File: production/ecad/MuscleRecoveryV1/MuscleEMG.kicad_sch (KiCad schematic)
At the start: 0 parts

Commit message: changes to fuel guage schematic and quick draft of ecg schematic - not finished
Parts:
- added C1, C2: 470n, symbol Device:C
- added C10, C4: 1n, symbol Device:C
- added C11: 100n, symbol Device:C
- added C3: 270p, symbol Device:C
- added D5, D6: LED, symbol Device:LED
- added J1: electrode 1, symbol Connector:Screw_Terminal_01x01
- added J2: electrode 2, symbol Connector:Screw_Terminal_01x01
- added J3: electrode 3, symbol Connector:Screw_Terminal_01x01
- added R1, R2: 200k, symbol Device:R
- added R19, R22: 180K, symbol Device:R
- added R20, R21: 2.2M, symbol Device:R
- added R23: 390K, symbol Device:R
- added R24, R28: 180, symbol Device:R
- added R25, R26, R5, R6: 1M, symbol Device:R
- added R27: 10k, symbol Device:R
- added R3: 27k, symbol Device:R
- added R4: 330k, symbol Device:R
- added R7: 100k, symbol Device:R
- added U5: AD8232ACPZ-R7, CP_20_10_ADI, symbol AD8232ACPZ-R7:AD8232ACPZ-R7
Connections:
- new net: C3.2, R4.2, R5.1
- new net: C1.1, U5.1 (HPDRIVE)
- new net: R27.1, U5.13 (*SDN)
- new net: R25.2, R26.1, U5.18 (REFIN)
- new net: R19.2, U5.2 (IN+)
- new net: C1.2, R1.1, U5.20 (HPSENSE)
- new net: R22.2, U5.3 (IN-)
- new net: C10.1, U5.4 (RLDFB)
- new net: C10.2, R23.2, U5.5 (RLD)
- new net: C4.2, R5.2, U5.7 (OPAMP+)
- new net: R6.2, R7.2, U5.9 (OPAMP-)
- new net: D6.1 (K), R28.1
- new net: J2.1 (Pin_1), R21.1, R22.1
- new net: D5.1 (K), R24.1
- new net: R1.2, R2.2, R3.1
- new net: J3.1 (Pin_1), R23.1
- new net: J1.1 (Pin_1), R19.1, R20.1
- new net GND: C11.2, R24.2, R26.2, R28.2, U5.14 (AC/*DC), U5.16 (GND)
- new net HP: R2.1, R4.1, U5.19 (IAOUT)
- new net REF: C2.2, C4.1, R7.1, U5.8 (REFOUT)
- new net SW: C2.1, R3.2, U5.6 (SW)
- new net VCC: C11.1, D6.2 (A), R20.2, R21.2, R25.1, R27.2, U5.15 (FR), U5.17 (VS+)
- new net Vout: C3.1, D5.2 (A), R6.1, U5.10 (OUT)
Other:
- note added: "High Pass: Fc = 10/(2piSQRT(R1R2C1C2)) R3 = 0.14R1"
- note added: "Low Pass: Fc = 10/(2piSQRT(R4R5C3C4)) Gain = 1 + R6 / R7"

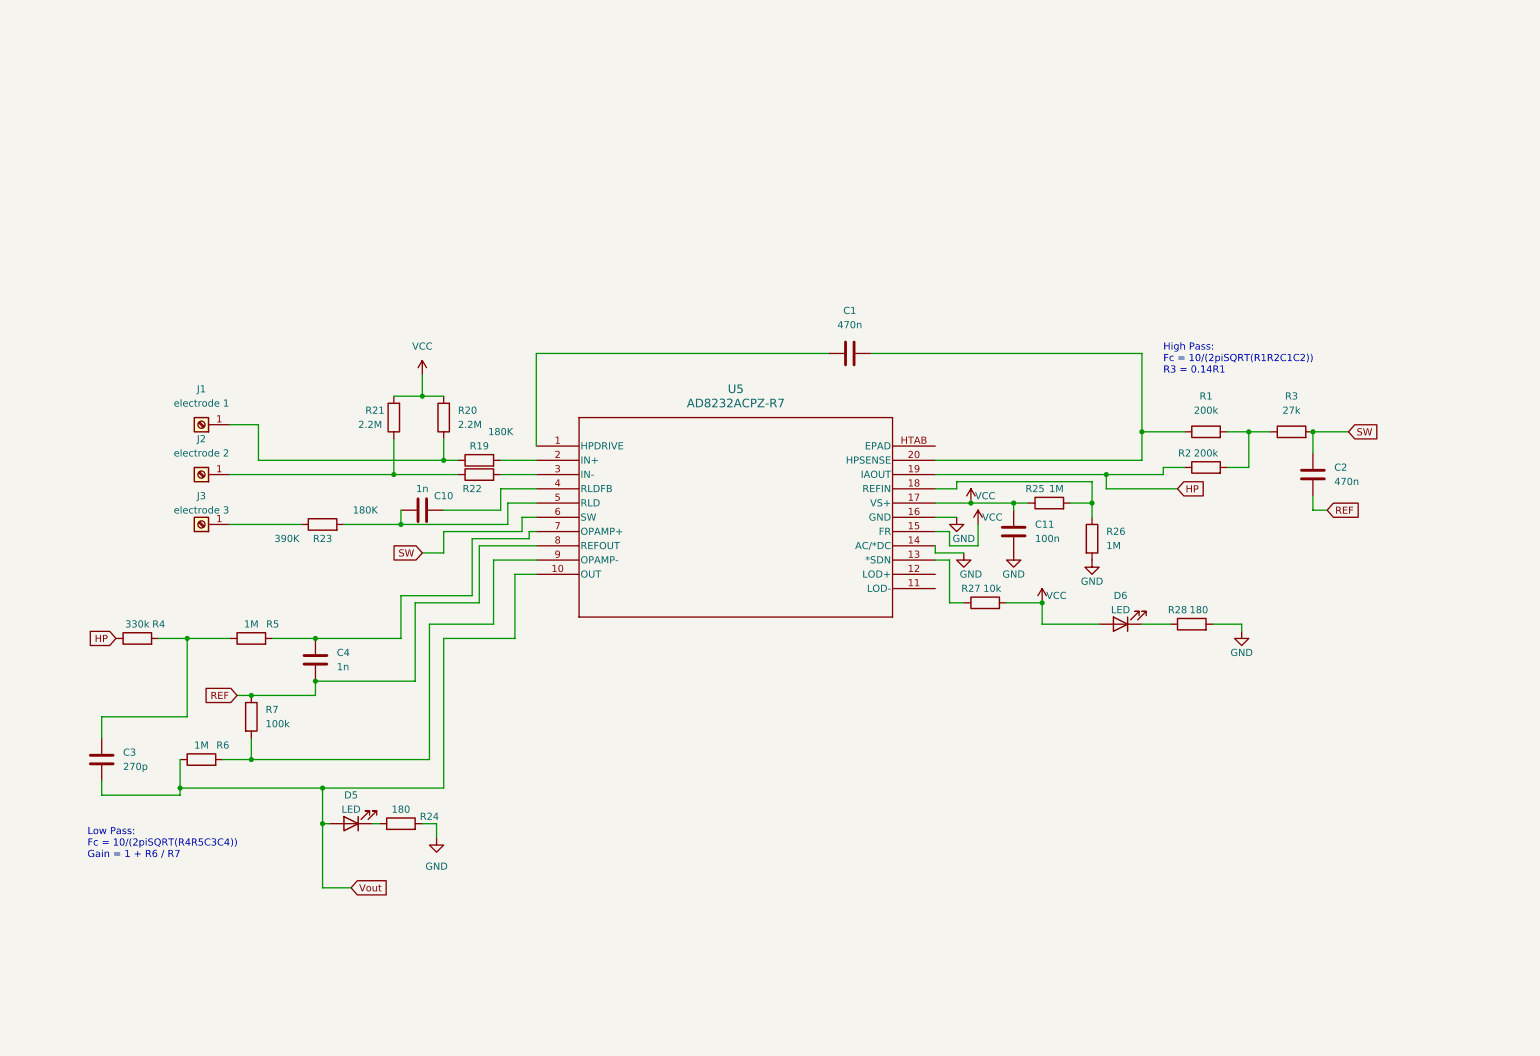
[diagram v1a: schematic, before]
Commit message: added ADS1115 schematic
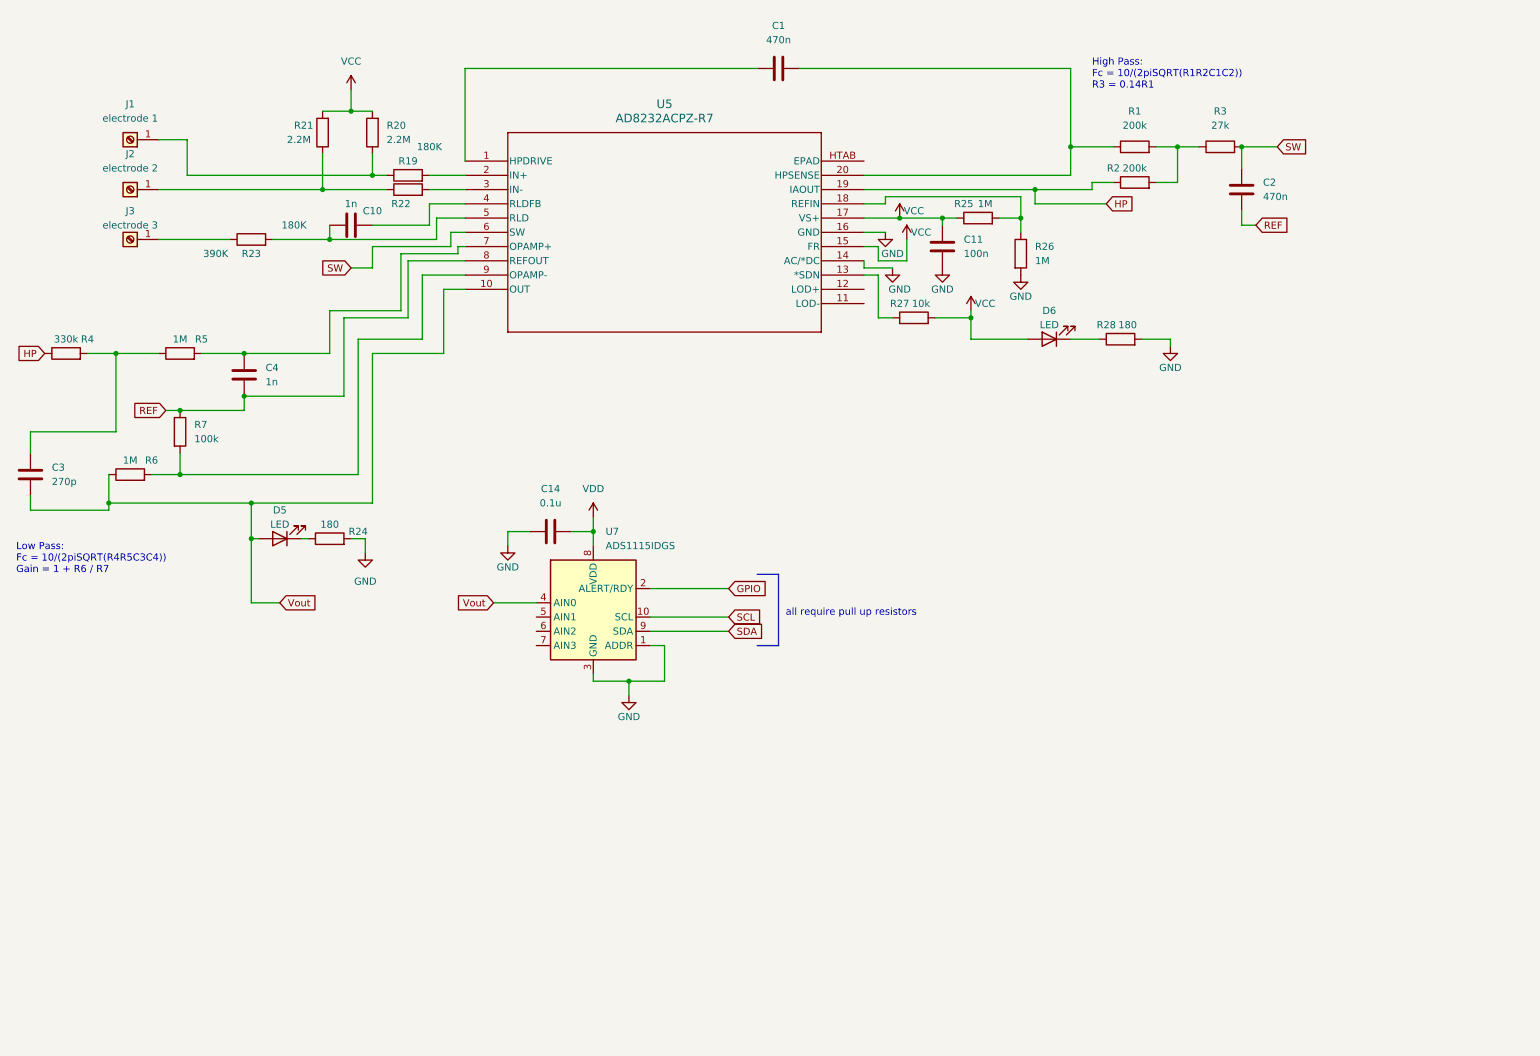
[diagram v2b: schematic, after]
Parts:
- added C14: 0.1u, symbol Device:C
- added U7: ADS1115IDGS, Package_SO:TSSOP-10_3x3mm_P0.5mm, symbol Analog_ADC:ADS1115IDGS
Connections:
- net GND: now also C14.1, U7.1 (ADDR), U7.3 (GND)
- net Vout: now also U7.4 (AIN0)
- new net GPIO: U7.2 (ALERT/RDY)
- new net SCL: U7.10 (SCL)
- new net SDA: U7.9 (SDA)
- new net VDD: C14.2, U7.8 (VDD)
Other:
- note added: "all require pull up resistors"
- moved on the sheet: C1, C10, C11, C2, C3, C4, D5, D6, J1, J2, J3, R1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

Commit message: cleaned up EMG
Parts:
- removed J1: electrode 1, symbol Connector:Screw_Terminal_01x01
- removed J2: electrode 2, symbol Connector:Screw_Terminal_01x01
- removed J3: electrode 3, symbol Connector:Screw_Terminal_01x01
- added J1: AudioJack3, symbol Connector_Audio:AudioJack3
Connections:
- net GND: now also U5.HTAB (EPAD)
- net RA: now reaches R21.1, R22.1
- net RA: now also J1.R
- net RL: now reaches R23.1
- net RL: now also J1.T
- net LA: now reaches R19.1, R20.1
- net LA: now also J1.S
- net VCC renamed +3V3
- no-connect marks 0 -> 2
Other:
- note added: "Audiojack. Connections must be configured."
- note added: "currently at 16.93Hz"
- note added: "currently at 533.189Hz"
- moved on the sheet: C1, C10, C11, C14, C2, C3, C4, D5, D6, R1, R19, R2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

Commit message: Labels and other stuff
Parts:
- added J2: Screw_Terminal_01x03, symbol Connector:Screw_Terminal_01x03
- added R29: 4.7k, symbol Device:R
- added Vout1: TestPoint, symbol Connector:TestPoint
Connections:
- net VDD is gone; now on net +3V3: C14.2, U7.8 (VDD)
- net +3V3: now also R29.1
- net LA: now also J2.3 (Pin_3)
- net RA: now also J2.2 (Pin_2)
- net RL: now also J2.1 (Pin_1)
- net Vout: now also Vout1.1
- net GPIO renamed ALERT/READY
- net ALERT/READY: now also R29.2
- no-connect marks 2 -> 5
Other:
- note added: "AD8232 Circuit"
- note added: "ADC"
- moved on the sheet: C1, C10, C11, C14, C2, C3, C4, D5, D6, J1, R1, R19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

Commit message: Display commit 1
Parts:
- removed J1: AudioJack3, symbol Connector_Audio:AudioJack3
- removed J2: Screw_Terminal_01x03, symbol Connector:Screw_Terminal_01x03
- removed R29: 4.7k, symbol Device:R
- removed Vout1: TestPoint, symbol Connector:TestPoint
- added J1: electrode 1, symbol Connector:Screw_Terminal_01x01
- added J2: electrode 2, symbol Connector:Screw_Terminal_01x01
- added J3: electrode 3, symbol Connector:Screw_Terminal_01x01
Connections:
- net GND: no longer U5.HTAB (EPAD)
- net +3V3 renamed VCC
- net VCC: no longer C14.2, U7.8 (VDD)
- net ALERT/READY renamed GPIO
- net LA: no longer names the net of R19.1, R20.1
- net LA: now also J1.1 (Pin_1)
- net RA: no longer names the net of R21.1, R22.1
- net RA: now also J2.1 (Pin_1)
- net RL: no longer names the net of R23.1
- net RL: now also J3.1 (Pin_1)
- new net VDD: C14.2, U7.8 (VDD)
- no-connect marks 5 -> 0
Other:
- note removed: "AD8232 Circuit"
- note removed: "ADC"
- note removed: "Audiojack. Connections must be configured."
- note removed: "currently at 16.93Hz"
- note removed: "currently at 533.189Hz"
- moved on the sheet: C1, C10, C11, C14, C2, C3, C4, D5, D6, R1, R19, R2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

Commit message: Revert "Display commit 1"
This reverts commit 52e50f7827ccbfa861bea7a8a003d131d02fed89.
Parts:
- removed J1: electrode 1, symbol Connector:Screw_Terminal_01x01
- removed J2: electrode 2, symbol Connector:Screw_Terminal_01x01
- removed J3: electrode 3, symbol Connector:Screw_Terminal_01x01
- added J1: AudioJack3, symbol Connector_Audio:AudioJack3
- added J2: Screw_Terminal_01x03, symbol Connector:Screw_Terminal_01x03
- added R29: 4.7k, symbol Device:R
- added Vout1: TestPoint, symbol Connector:TestPoint
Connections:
- net VDD is gone; now on net +3V3: C14.2, U7.8 (VDD)
- net GND: now also U5.HTAB (EPAD)
- net Vout: now also Vout1.1
- net RA: now reaches R21.1, R22.1
- net RA: now also J1.R, J2.2 (Pin_2)
- net RL: now reaches R23.1
- net RL: now also J1.T, J2.1 (Pin_1)
- net LA: now reaches R19.1, R20.1
- net LA: now also J1.S, J2.3 (Pin_3)
- net GPIO renamed ALERT/READY
- net ALERT/READY: now also R29.2
- net VCC renamed +3V3
- net +3V3: now also R29.1
- no-connect marks 0 -> 5
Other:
- note added: "AD8232 Circuit"
- note added: "ADC"
- note added: "Audiojack. Connections must be configured."
- note added: "currently at 16.93Hz"
- note added: "currently at 533.189Hz"
- moved on the sheet: C1, C10, C11, C14, C2, C3, C4, D5, D6, R1, R19, R2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

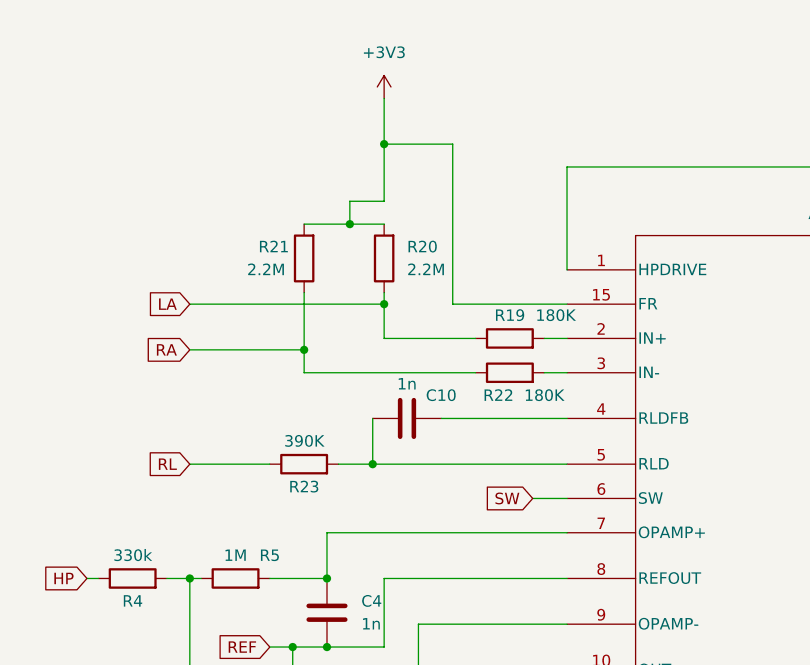
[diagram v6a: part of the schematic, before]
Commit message: updates from Sean's comments, some not all
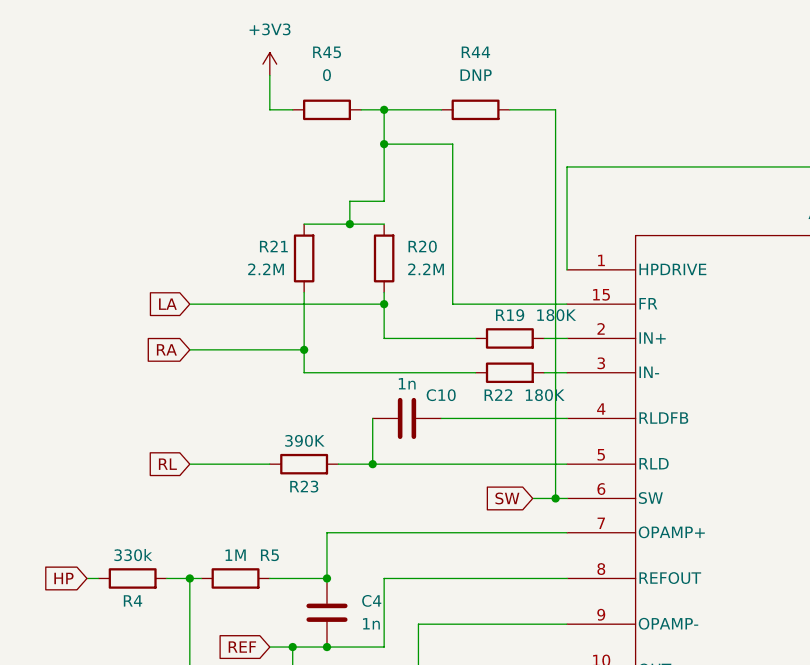
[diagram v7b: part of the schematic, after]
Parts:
- added R44: DNP, symbol Device:R
- added R45: 0, symbol Device:R
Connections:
- net +3V3: now also R45.1; no longer R20.2, R21.2, U5.15 (FR)
- net SW: now also R44.2
- new net: R20.2, R21.2, R44.1, R45.2, U5.15 (FR)
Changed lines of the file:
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@@
   (junction (at 124.46 35.56) (diameter 0) (color 0 0 0 0)
   )
+  (junction (at 128.27 22.86) (diameter 0) (color 0 0 0 0)
+  )
   (junction (at 137.16 102.87) (diameter 0) (color 0 0 0 0)
   )
@@
   )
   (junction (at 118.11 82.55) (diameter 0) (color 0 0 0 0)
+  )
+  (junction (at 147.32 66.04) (diameter 0) (color 0 0 0 0)
   )
   (junction (at 245.11 55.88) (diameter 0) (color 0 0 0 0)
@@
     (stroke (width 0) (type default))
   )
+  (wire (pts (xy 147.32 66.04) (xy 148.59 66.04))
+    (stroke (width 0) (type default))
+  )
   (wire (pts (xy 100.33 102.87) (xy 109.22 102.87))
     (stroke (width 0) (type default))
@@
     (stroke (width 0) (type default))
   )
+  (wire (pts (xy 147.32 66.04) (xy 147.32 22.86))
+    (stroke (width 0) (type default))
+  )
   (wire (pts (xy 45.72 156.21) (xy 45.72 158.75))
     (stroke (width 0) (type default))
@@
     (stroke (width 0) (type default))
   )
+  (wire (pts (xy 147.32 22.86) (xy 142.24 22.86))
+    (stroke (width 0) (type default))
+  )
   (wire (pts (xy 137.16 102.87) (xy 137.16 105.41))
     (stroke (width 0) (type default))
@@
     (stroke (width 0) (type default))
   )
-  (wire (pts (xy 128.27 21.59) (xy 128.27 26.67))
+  (wire (pts (xy 115.57 19.05) (xy 115.57 22.86))
     (stroke (width 0) (type default))
   )
@@
     (stroke (width 0) (type default))
   )
+  (wire (pts (xy 128.27 22.86) (xy 128.27 26.67))
+    (stroke (width 0) (type default))
+  )
   (wire (pts (xy 106.68 44.45) (xy 128.27 44.45))
     (stroke (width 0) (type default))
   )
+  (wire (pts (xy 128.27 22.86) (xy 134.62 22.86))
+    (stroke (width 0) (type default))
+  )
   (wire (pts (xy 127 62.23) (xy 148.59 62.23))
     (stroke (width 0) (type default))
   )
-  (wire (pts (xy 144.78 66.04) (xy 148.59 66.04))
+  (wire (pts (xy 144.78 66.04) (xy 147.32 66.04))
     (stroke (width 0) (type default))
   )
@@
     (stroke (width 0) (type default))
   )
+  (wire (pts (xy 115.57 22.86) (xy 118.11 22.86))
+    (stroke (width 0) (type default))
+  )
   (wire (pts (xy 35.56 91.44) (xy 41.91 91.44))
     (stroke (width 0) (type default))
@@
   )
   (wire (pts (xy 109.22 96.52) (xy 109.22 102.87))
+    (stroke (width 0) (type default))
+  )
+  (wire (pts (xy 125.73 22.86) (xy 128.27 22.86))
     (stroke (width 0) (type default))
   )
@@
     )
   )
-  (symbol (lib_id "power:+3V3") (at 128.27 21.59 0) (unit 1)
+  (symbol (lib_id "Device:R") (at 138.43 22.86 90) (unit 1)
     (in_bom yes) (on_board yes) (dnp no) (fields_autoplaced)
-    (property "Reference" "#PWR058" (at 128.27 25.4 0)
-      (effects (font (size 1.27 1.27)) hide)
-    )
-    (property "Value" "+3V3" (at 128.27 16.51 0)
-      (effects (font (size 1.27 1.27)))
-    )
-    (property "Footprint" "" (at 128.27 21.59 0)
-      (effects (font (size 1.27 1.27)) hide)
-    )
-    (property "Datasheet" "" (at 128.27 21.59 0)
+    (property "Reference" "R44" (at 138.43 16.51 90)
+      (effects (font (size 1.27 1.27)))
+    )
+    (property "Value" "DNP" (at 138.43 19.05 90)
+      (effects (font (size 1.27 1.27)))
+    )
+    (property "Footprint" "" (at 138.43 24.638 90)
+      (effects (font (size 1.27 1.27)) hide)
+    )
+    (property "Datasheet" "~" (at 138.43 22.86 0)
+      (effects (font (size 1.27 1.27)) hide)
+    )
+    (pin "1")
+    (pin "2")
+    (instances
+      (project "MuscleRecoveryV1"
+        (path "/4e550305-79d2-4e4a-a502-817ebcc79f9a/284c60dd-e199-4b03-b99f-cc7eaed256f8"
+          (reference "R44") (unit 1)
+        )
+      )
+    )
+  )
+  (symbol (lib_id "power:+3V3") (at 115.57 19.05 0) (unit 1)
+    (in_bom yes) (on_board yes) (dnp no) (fields_autoplaced)
+    (property "Reference" "#PWR058" (at 115.57 22.86 0)
+      (effects (font (size 1.27 1.27)) hide)
+    )
+    (property "Value" "+3V3" (at 115.57 13.97 0)
+      (effects (font (size 1.27 1.27)))
+    )
+    (property "Footprint" "" (at 115.57 19.05 0)
+      (effects (font (size 1.27 1.27)) hide)
+    )
+    (property "Datasheet" "" (at 115.57 19.05 0)
       (effects (font (size 1.27 1.27)) hide)
     )
@@
         )
       )
+    )
+  )
+  (symbol (lib_id "Device:R") (at 121.92 22.86 90) (unit 1)
+    (in_bom yes) (on_board yes) (dnp no) (fields_autoplaced)
+    (property "Reference" "R45" (at 121.92 16.51 90)
+      (effects (font (size 1.27 1.27)))
+    )
+    (property "Value" "0" (at 121.92 19.05 90)
+      (effects (font (size 1.27 1.27)))
+    )
+    (property "Footprint" "" (at 121.92 24.638 90)
+      (effects (font (size 1.27 1.27)) hide)
+    )
+    (property "Datasheet" "~" (at 121.92 22.86 0)
+      (effects (font (size 1.27 1.27)) hide)
+    )
+    (pin "1")
+    (pin "2")
+    (instances
+      (project "MuscleRecoveryV1"
+        (path "/4e550305-79d2-4e4a-a502-817ebcc79f9a/284c60dd-e199-4b03-b99f-cc7eaed256f8"
+          (reference "R45") (unit 1)
+        )
+      )

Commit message: some emg changes
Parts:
- removed Vout1: TestPoint, symbol Connector:TestPoint
- added J5: Screw_Terminal_01x04, symbol Connector:Screw_Terminal_01x04
- added R46: 1k, symbol Device:R
- added R47, R48, R49: 0, symbol Device:R
- C1, C10, C11, C14, C2, C3, C4: footprint (none) -> Capacitor_SMD:C_0805_2012Metric
- R1, R19, R2, R20, R21, R22, R23, R25, R26, R27, R28, R29, R3, R4, R44, R45, R5, R6, R7: footprint (none) -> Resistor_SMD:R_0805_2012Metric
- R24: value 180 -> 0
- U5: footprint CP_20_10_ADI -> AD8232ACPZ-R7:CP_20_10_ADI
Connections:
- net ALERT/READY: now also R49.2; no longer U7.2 (ALERT/RDY)
- net HP: now also J5.1 (Pin_1)
- net SCL: now also R47.2; no longer U7.10 (SCL)
- net SDA: now also R48.2; no longer U7.9 (SDA)
- net Vout: now also J5.2 (Pin_2), R46.1; no longer D5.2 (A)
- net LOD-: now reaches U5.11 (LOD-)
- net LOD-: now also J5.4 (Pin_4)
- net LOD+: now reaches U5.12 (LOD+)
- net LOD+: now also J5.3 (Pin_3)
- new net: R47.1, U7.10 (SCL)
- new net: R49.1, U7.2 (ALERT/RDY)
- new net: R48.1, U7.9 (SDA)
- new net: D5.2 (A), R46.2
- no-connect marks 5 -> 3
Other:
- moved on the sheet: D5
